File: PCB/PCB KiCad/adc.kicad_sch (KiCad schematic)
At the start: 0 parts

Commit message: draw schematic for 60%
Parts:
- added C? (x5): C, Capacitor_SMD:C_0805_2012Metric_Pad1.18x1.45mm_HandSolder, symbol Device:C
- added R? (x11): R, Resistor_SMD:R_0805_2012Metric_Pad1.20x1.40mm_HandSolder, symbol Device:R
- added U?: ADS1256IDBT, ADS1256:Texas_Instruments-ADS1256IDBT-Level_A, symbol ADS1256:ADS1256IDBT
- added Y?: Crystal, symbol Device:Crystal
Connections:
- new net: R?.1, U?.23 (DIN)
- new net: C?.1, C?.1, C?.1, R?.2, U?.4 (VREFP)
- new net: R?.1, U?.24 (SCLK)
- new net: C?.1, U?.18 (XTAL2), Y?.1
- new net: C?.1, U?.19 (XTAL1/CLKIN), Y?.2
- new net: R?.1, U?.20 (~{CS})
- new net: R?.1, U?.14 (~{SYNC}/~{PDWN})
- new net: R?.1, U?.15 (~{RESET})
- new net: R?.1, U?.21 (~{DRDY})
- new net: R?.1, U?.22 (DOUT)
- new net: C?.2, C?.2, C?.2, R?.2, U?.3 (VREFN)
- new net: R?.2, R?.2 (x2)
- new net +3V3: R?.1, R?.1, U?.16 (DVDD)
- new net +5V: U?.1 (AVDD)
- new net GND: C?.2, C?.2, R?.1, U?.17 (DGND), U?.2 (AGND), U?.5 (AINCOM)
- no-connect marks 0 -> 10
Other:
- note added: "TO DO: Nets Values"

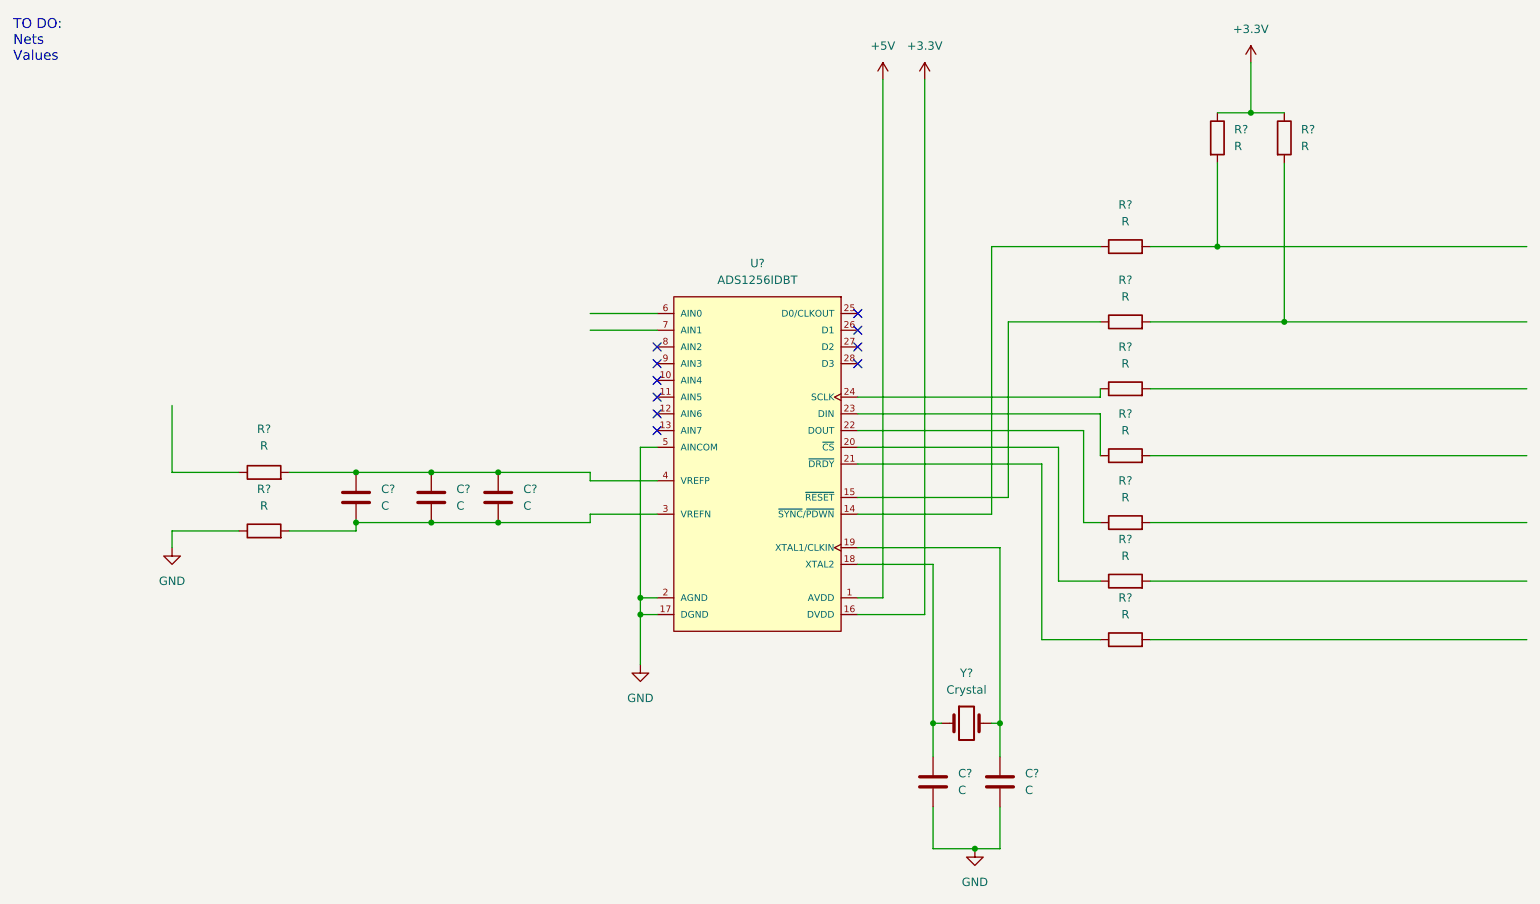
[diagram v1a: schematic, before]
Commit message: Add buttons: MCU RESET, TRIGGER
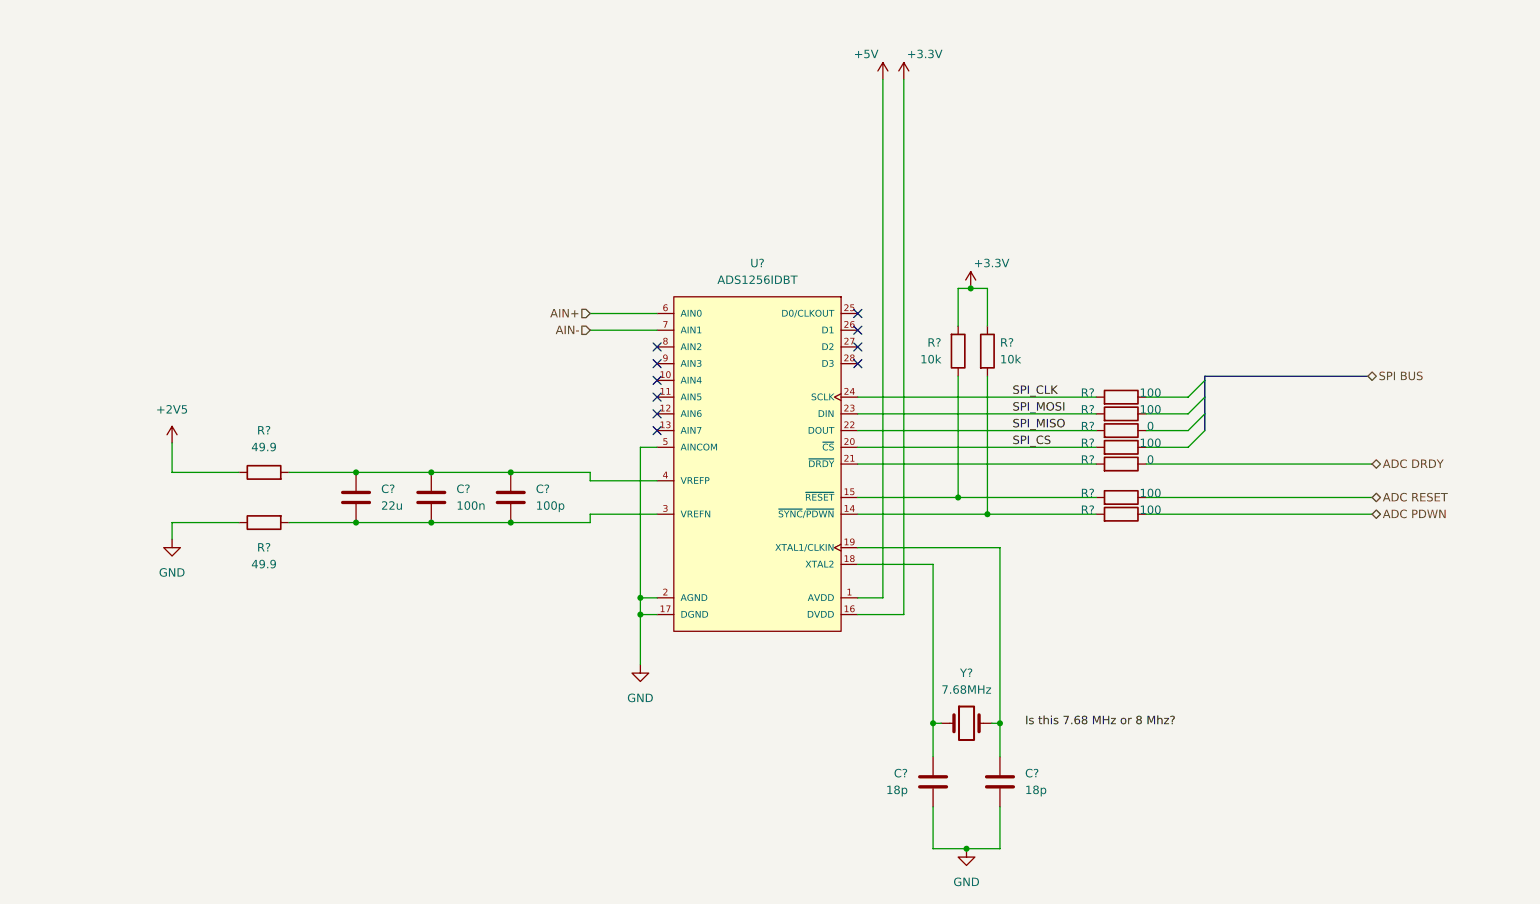
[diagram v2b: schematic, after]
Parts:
- removed R? (x9): R, Resistor_SMD:R_0805_2012Metric_Pad1.20x1.40mm_HandSolder, symbol Device:R
- added R? (x2): 10k, symbol Device:R
- added R? (x5): 100, symbol Device:R
- added R? (x2): 0, symbol Device:R
- C?: value C -> 100n
- C? (x2): value C -> 18p
- C?: value C -> 100p
- C?: value C -> 22u
- R? (x2): value R -> 49.9
- Y?: value Crystal -> 7.68MHz
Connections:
- net +3V3: now also R?.1, R?.2
- net GND: now also C?.1; no longer C?.2
- net SPI_MOSI: now reaches U?.23 (DIN)
- net SPI_MOSI: now also R?.2
- net +2V5: now reaches R?.1
- net SPI_CLK: now reaches U?.24 (SCLK)
- net SPI_CLK: now also R?.2
- net at U?.18 (XTAL2), Y?.1: now also C?.2; no longer C?.1
- net SPI_CS: now reaches U?.20 (~{CS})
- net SPI_CS: now also R?.2
- net at U?.14 (~{SYNC}/~{PDWN}): now also R?.2, R?.2
- net at U?.15 (~{RESET}): now also R?.1, R?.2
- net at U?.21 (~{DRDY}): now also R?.2
- net SPI_MISO: now reaches U?.22 (DOUT)
- net SPI_MISO: now also R?.2
- net AIN+: now reaches U?.6 (AIN0)
- net AIN-: now reaches U?.7 (AIN1)
- new net ADC DRDY: R?.1
- new net ADC PDWN: R?.1
- new net ADC RESET: R?.1
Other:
- note removed: "TO DO: Nets Values"
- moved on the sheet: C?, R?

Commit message: first check + add connectors
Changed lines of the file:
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@@
-    (effects (font (size 1.27 1.27)) (justify left bottom))
-  )
-  (label "Is this 7.68 MHz or 8 Mhz?" (at 198.12 132.715 0)
     (effects (font (size 1.27 1.27)) (justify left bottom))
   )

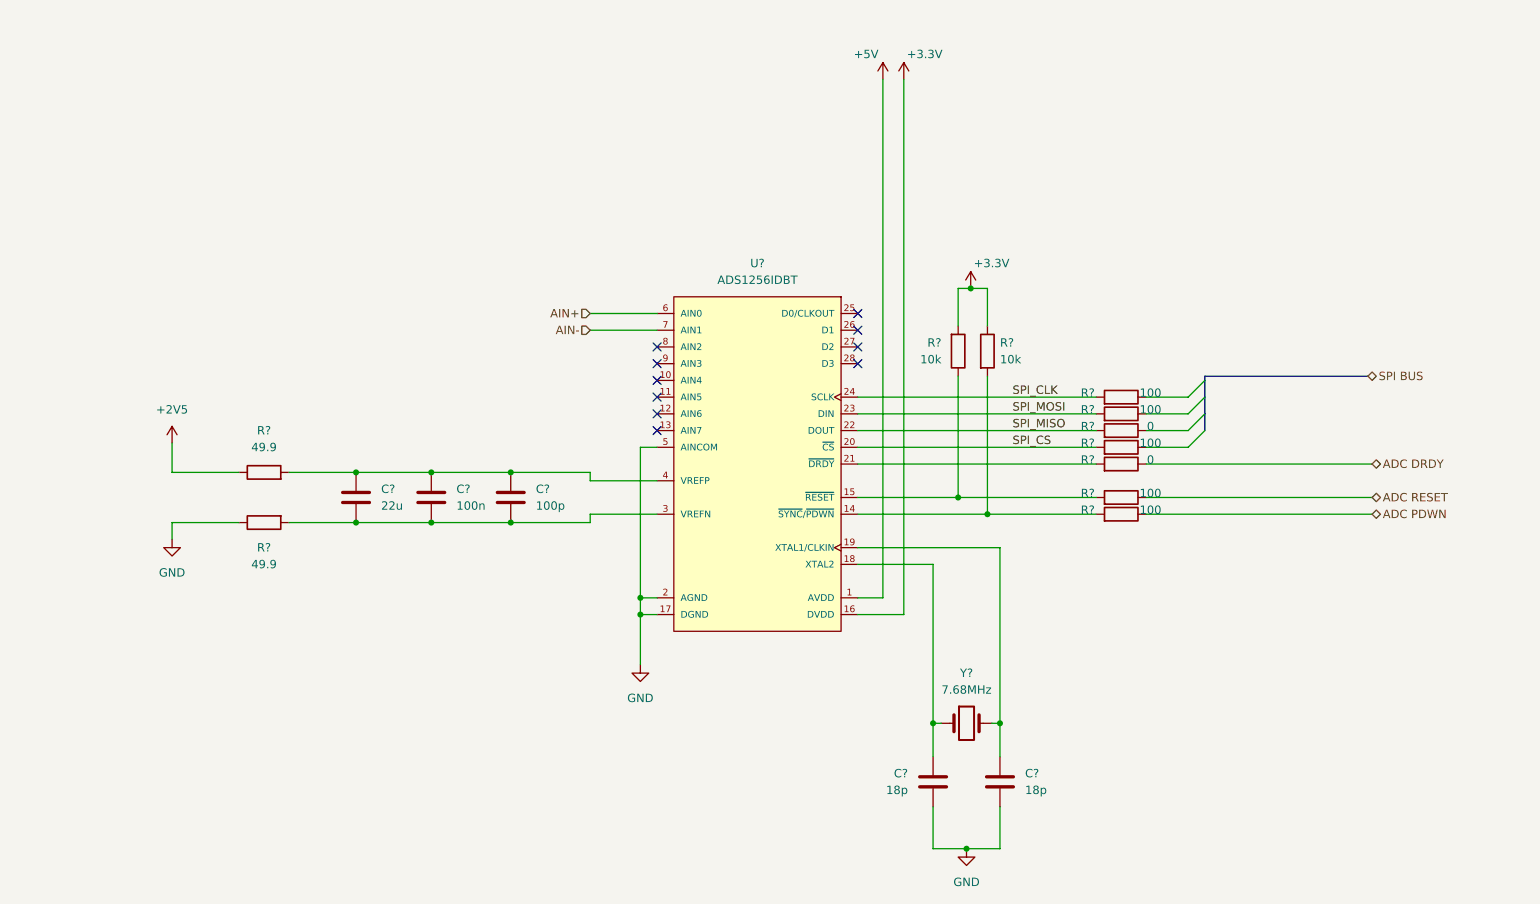
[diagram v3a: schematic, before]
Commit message: ERC: add power flags to satisfy the ERC crap
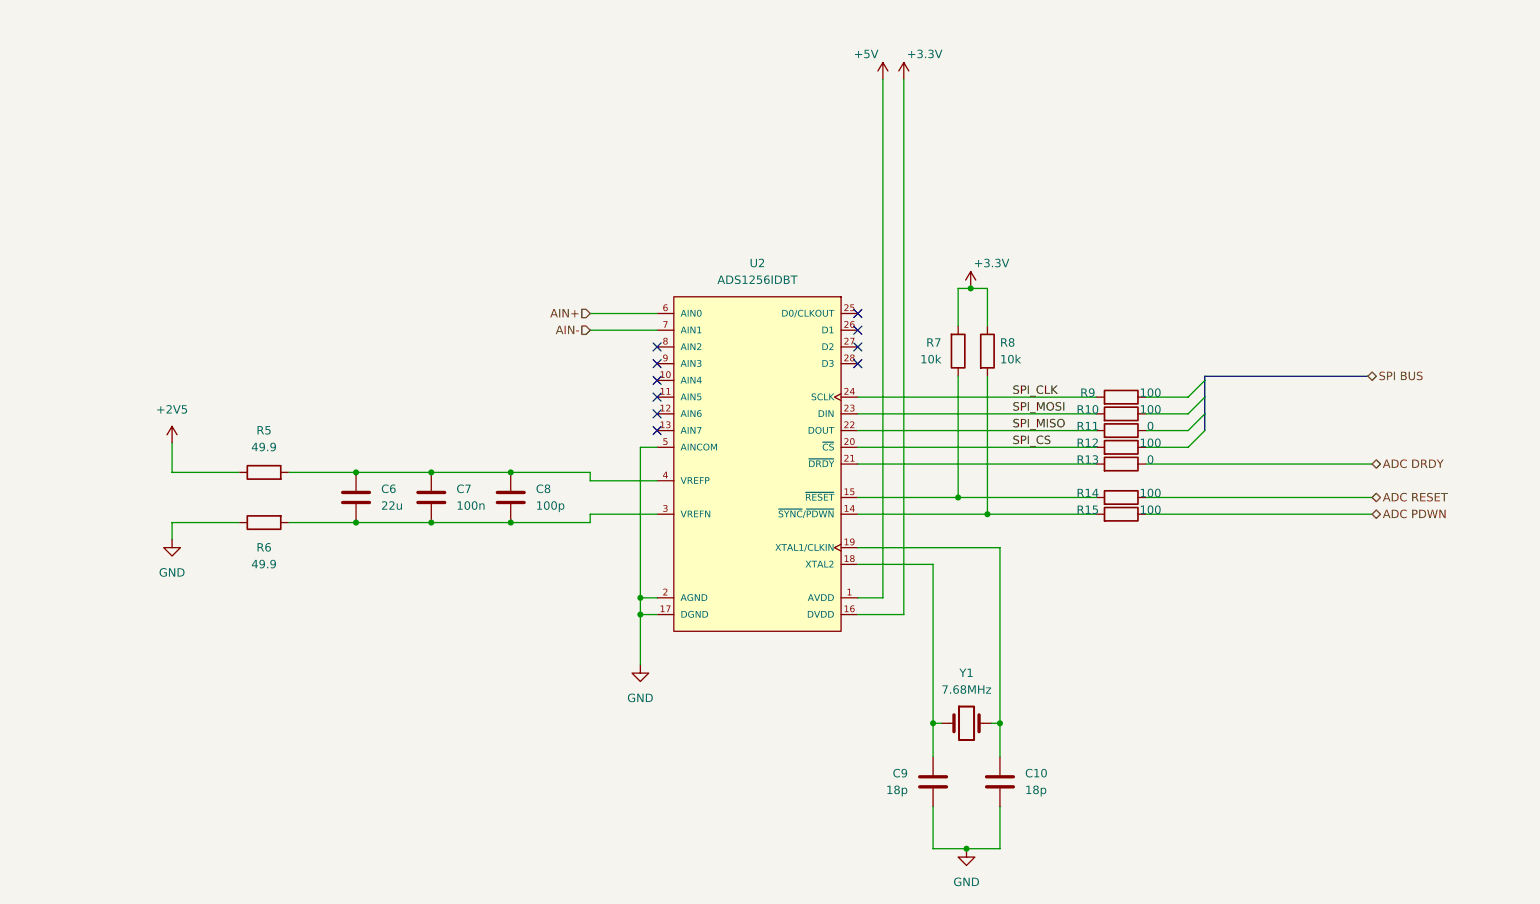
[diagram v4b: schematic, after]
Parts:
- gave numbers to parts that had none: 18
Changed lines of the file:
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@@
   (symbol (lib_id "Device:R") (at 82.55 93.98 90) (unit 1)
     (in_bom yes) (on_board yes) (fields_autoplaced)
-    (property "Reference" "R?" (id 0) (at 82.55 87.63 90))
+    (property "Reference" "R5" (id 0) (at 82.55 87.63 90))
     (property "Value" "49.9" (id 1) (at 82.55 90.17 90))
     (property "Footprint" "Resistor_SMD:R_0805_2012Metric_Pad1.20x1.40mm_HandSolder" (id 2) (at 82.55 95.758 90)
@@
   (symbol (lib_id "power:GND") (at 68.58 104.14 0) (unit 1)
     (in_bom yes) (on_board yes) (fields_autoplaced)
-    (property "Reference" "#PWR?" (id 0) (at 68.58 110.49 0)
+    (property "Reference" "#PWR06" (id 0) (at 68.58 110.49 0)
       (effects (font (size 1.27 1.27)) hide)
     )
@@
   (symbol (lib_id "power:GND") (at 139.7 123.19 0) (unit 1)
     (in_bom yes) (on_board yes) (fields_autoplaced)
-    (property "Reference" "#PWR?" (id 0) (at 139.7 129.54 0)
+    (property "Reference" "#PWR07" (id 0) (at 139.7 129.54 0)
       (effects (font (size 1.27 1.27)) hide)
     )
@@
   (symbol (lib_id "Device:Crystal") (at 189.23 132.08 0) (unit 1)
     (in_bom yes) (on_board yes) (fields_autoplaced)
-    (property "Reference" "Y?" (id 0) (at 189.23 124.46 0))
+    (property "Reference" "Y1" (id 0) (at 189.23 124.46 0))
     (property "Value" "7.68MHz" (id 1) (at 189.23 127 0))
     (property "Footprint" "" (id 2) (at 189.23 132.08 0)
@@
   (symbol (lib_id "ADS1256:ADS1256IDBT") (at 175.26 69.85 0) (mirror y) (unit 1)
     (in_bom yes) (on_board yes) (fields_autoplaced)
-    (property "Reference" "U?" (id 0) (at 157.48 62.23 0))
+    (property "Reference" "U2" (id 0) (at 157.48 62.23 0))
     (property "Value" "ADS1256IDBT" (id 1) (at 157.48 64.77 0))
     (property "Footprint" "ADS1256:Texas_Instruments-ADS1256IDBT-Level_A" (id 2) (at 175.26 59.69 0)
@@
   (symbol (lib_id "power:+5V") (at 176.53 34.29 0) (unit 1)
     (in_bom yes) (on_board yes)
-    (property "Reference" "#PWR?" (id 0) (at 176.53 38.1 0)
+    (property "Reference" "#PWR08" (id 0) (at 176.53 38.1 0)
       (effects (font (size 1.27 1.27)) hide)
     )
@@
   (symbol (lib_id "Device:R") (at 192.405 75.565 0) (unit 1)
     (in_bom yes) (on_board yes) (fields_autoplaced)
-    (property "Reference" "R?" (id 0) (at 194.31 74.2949 0)
+    (property "Reference" "R8" (id 0) (at 194.31 74.2949 0)
       (effects (font (size 1.27 1.27)) (justify left))
     )
@@
   (symbol (lib_id "Device:C") (at 107.95 97.79 0) (unit 1)
     (in_bom yes) (on_board yes) (fields_autoplaced)
-    (property "Reference" "C?" (id 0) (at 111.76 96.5199 0)
+    (property "Reference" "C7" (id 0) (at 111.76 96.5199 0)
       (effects (font (size 1.27 1.27)) (justify left))
     )
@@
   (symbol (lib_id "Device:R") (at 187.96 75.565 0) (mirror x) (unit 1)
     (in_bom yes) (on_board yes) (fields_autoplaced)
-    (property "Reference" "R?" (id 0) (at 185.42 74.2949 0)
+    (property "Reference" "R7" (id 0) (at 185.42 74.2949 0)
       (effects (font (size 1.27 1.27)) (justify right))
     )
@@
   (symbol (lib_id "Device:C") (at 184.15 140.97 0) (mirror x) (unit 1)
     (in_bom yes) (on_board yes) (fields_autoplaced)
-    (property "Reference" "C?" (id 0) (at 180.34 139.6999 0)
+    (property "Reference" "C9" (id 0) (at 180.34 139.6999 0)
       (effects (font (size 1.27 1.27)) (justify right))
     )
@@
   (symbol (lib_id "Device:R") (at 212.725 90.17 270) (mirror x) (unit 1)
     (in_bom yes) (on_board yes)
-    (property "Reference" "R?" (id 0) (at 207.645 89.535 90))
+    (property "Reference" "R12" (id 0) (at 207.645 89.535 90))
     (property "Value" "100" (id 1) (at 217.17 89.535 90))
     (property "Footprint" "" (id 2) (at 212.725 91.948 90)
@@
   (symbol (lib_id "Device:R") (at 82.55 101.6 90) (mirror x) (unit 1)
     (in_bom yes) (on_board yes)
-    (property "Reference" "R?" (id 0) (at 82.55 105.41 90))
+    (property "Reference" "R6" (id 0) (at 82.55 105.41 90))
     (property "Value" "49.9" (id 1) (at 82.55 107.95 90))
     (property "Footprint" "Resistor_SMD:R_0805_2012Metric_Pad1.20x1.40mm_HandSolder" (id 2) (at 82.55 99.822 90)
@@
   (symbol (lib_id "Device:C") (at 120.015 97.79 0) (unit 1)
     (in_bom yes) (on_board yes) (fields_autoplaced)
-    (property "Reference" "C?" (id 0) (at 123.825 96.5199 0)
+    (property "Reference" "C8" (id 0) (at 123.825 96.5199 0)
       (effects (font (size 1.27 1.27)) (justify left))
     )
@@
   (symbol (lib_id "power:+3.3V") (at 189.865 66.04 0) (unit 1)
     (in_bom yes) (on_board yes)
-    (property "Reference" "#PWR?" (id 0) (at 189.865 69.85 0)
+    (property "Reference" "#PWR011" (id 0) (at 189.865 69.85 0)
       (effects (font (size 1.27 1.27)) hide)
     )
@@
   (symbol (lib_id "Device:R") (at 212.725 97.79 270) (mirror x) (unit 1)
     (in_bom yes) (on_board yes)
-    (property "Reference" "R?" (id 0) (at 207.645 97.155 90))
+    (property "Reference" "R14" (id 0) (at 207.645 97.155 90))
     (property "Value" "100" (id 1) (at 217.17 97.155 90))
     (property "Footprint" "" (id 2) (at 212.725 99.568 90)
@@
   (symbol (lib_id "Device:R") (at 212.725 100.33 270) (mirror x) (unit 1)
     (in_bom yes) (on_board yes)
-    (property "Reference" "R?" (id 0) (at 207.645 99.695 90))
+    (property "Reference" "R15" (id 0) (at 207.645 99.695 90))
     (property "Value" "100" (id 1) (at 217.17 99.695 90))
     (property "Footprint" "" (id 2) (at 212.725 102.108 90)
@@
   (symbol (lib_id "Device:R") (at 212.725 85.09 270) (mirror x) (unit 1)
     (in_bom yes) (on_board yes)
-    (property "Reference" "R?" (id 0) (at 207.645 84.455 90))
+    (property "Reference" "R10" (id 0) (at 207.645 84.455 90))
     (property "Value" "100" (id 1) (at 217.17 84.455 90))
     (property "Footprint" "" (id 2) (at 212.725 86.868 90)
@@
   (symbol (lib_id "Device:R") (at 212.725 92.71 270) (mirror x) (unit 1)
     (in_bom yes) (on_board yes)
-    (property "Reference" "R?" (id 0) (at 207.645 92.075 90))
+    (property "Reference" "R13" (id 0) (at 207.645 92.075 90))
     (property "Value" "0" (id 1) (at 217.17 92.075 90))
     (property "Footprint" "" (id 2) (at 212.725 94.488 90)
@@
   (symbol (lib_id "Device:C") (at 194.31 140.97 0) (unit 1)
     (in_bom yes) (on_board yes) (fields_autoplaced)
-    (property "Reference" "C?" (id 0) (at 198.12 139.6999 0)
+    (property "Reference" "C10" (id 0) (at 198.12 139.6999 0)
       (effects (font (size 1.27 1.27)) (justify left))
     )
@@
   (symbol (lib_id "Device:C") (at 96.52 97.79 0) (unit 1)
     (in_bom yes) (on_board yes) (fields_autoplaced)
-    (property "Reference" "C?" (id 0) (at 100.33 96.5199 0)
+    (property "Reference" "C6" (id 0) (at 100.33 96.5199 0)
       (effects (font (size 1.27 1.27)) (justify left))
     )
@@
   (symbol (lib_id "power:+2V5") (at 68.58 89.535 0) (unit 1)
     (in_bom yes) (on_board yes) (fields_autoplaced)
-    (property "Reference" "#PWR?" (id 0) (at 68.58 93.345 0)
+    (property "Reference" "#PWR05" (id 0) (at 68.58 93.345 0)
       (effects (font (size 1.27 1.27)) hide)
     )
@@
   (symbol (lib_id "power:GND") (at 189.23 151.13 0) (unit 1)
     (in_bom yes) (on_board yes) (fields_autoplaced)
-    (property "Reference" "#PWR?" (id 0) (at 189.23 157.48 0)
+    (property "Reference" "#PWR010" (id 0) (at 189.23 157.48 0)
       (effects (font (size 1.27 1.27)) hide)
     )
@@
   (symbol (lib_id "Device:R") (at 212.725 87.63 270) (mirror x) (unit 1)
     (in_bom yes) (on_board yes)
-    (property "Reference" "R?" (id 0) (at 207.645 86.995 90))
+    (property "Reference" "R11" (id 0) (at 207.645 86.995 90))
     (property "Value" "0" (id 1) (at 217.17 86.995 90))
     (property "Footprint" "" (id 2) (at 212.725 89.408 90)
@@
   (symbol (lib_id "Device:R") (at 212.725 82.55 270) (mirror x) (unit 1)
     (in_bom yes) (on_board yes)
-    (property "Reference" "R?" (id 0) (at 207.645 81.915 90))
+    (property "Reference" "R9" (id 0) (at 207.645 81.915 90))
     (property "Value" "100" (id 1) (at 217.17 81.915 90))
     (property "Footprint" "" (id 2) (at 212.725 84.328 90)
@@
   (symbol (lib_id "power:+3.3V") (at 179.705 34.29 0) (unit 1)
     (in_bom yes) (on_board yes)
-    (property "Reference" "#PWR?" (id 0) (at 179.705 38.1 0)
-      (effects (font (size 1.27 1.27)) hide)
-    )
+    (property "Reference" "#PWR09" (id 0) (at 179.705 38.1 0)
+      (effects (font (size 1.27 1.27)) hide)
+    )
